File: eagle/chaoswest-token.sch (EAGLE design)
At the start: 40 parts, among them J2 CON_HEADER_PRG_AVR_ICSP-SMD, Q1 Si1967DH, SW1 SSAJ120100, U1 MCP73832T-2ACI/OT, U2 ATTINY85V-10SU, U3 MCP9700AT-E/LT

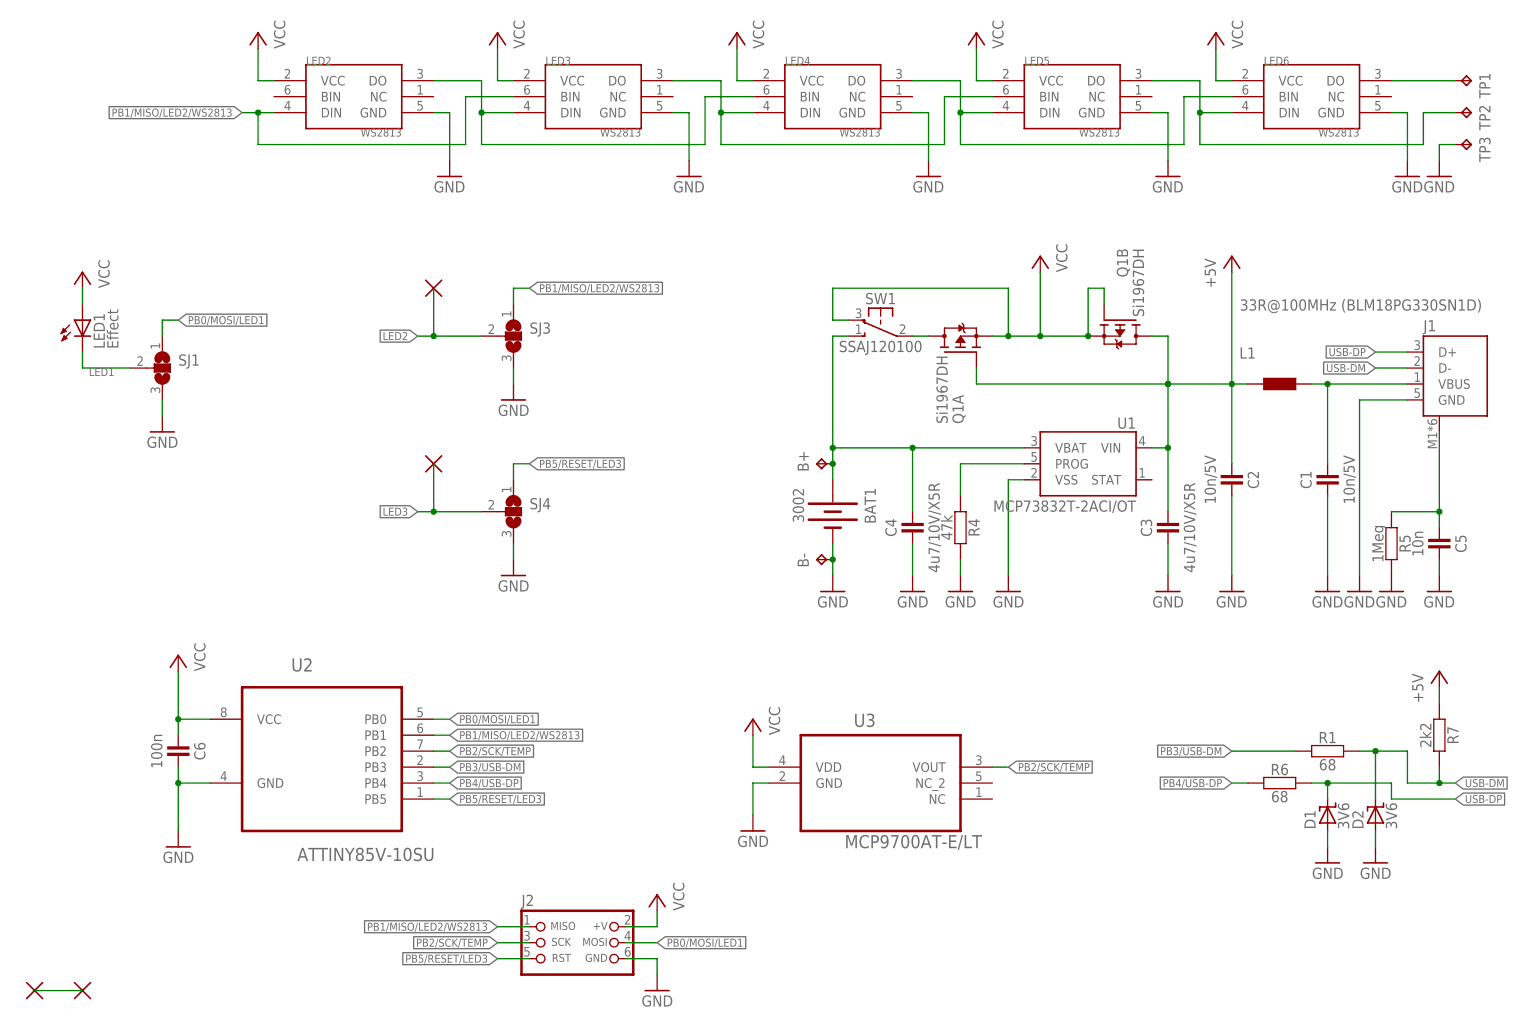
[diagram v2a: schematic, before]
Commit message: routing finished, single layer layout
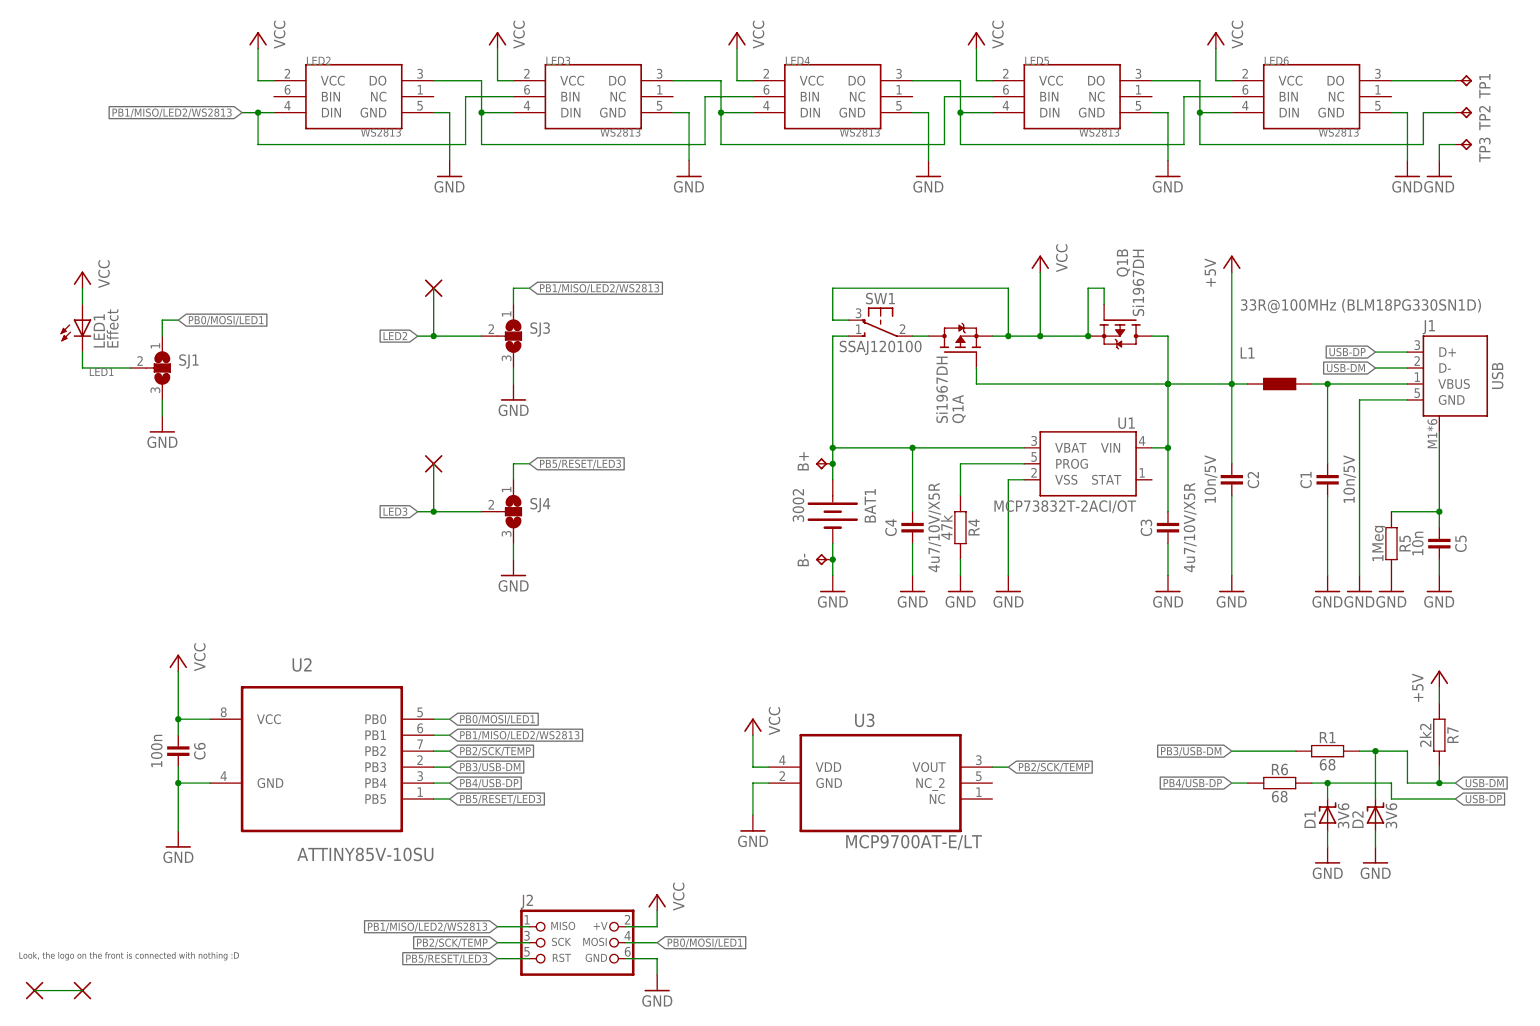
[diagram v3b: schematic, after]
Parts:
- J1: value (none) -> USB
- J2: value CON_HEADER_PRG_AVR_ICSP-SMD -> ISP
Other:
- note added: "Look, the logo on the front is connected with nothing :D"
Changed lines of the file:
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@@
 <layer number="97" name="Info" color="7" fill="1" visible="yes" active="yes"/>
 <layer number="98" name="Guide" color="6" fill="1" visible="yes" active="yes"/>
-<layer number="99" name="SpiceOrder" color="5" fill="1" visible="yes" active="yes"/>
 <layer number="100" name="Muster" color="7" fill="1" visible="no" active="no"/>
-<layer number="101" name="Patch_Top" color="12" fill="4" visible="yes" active="yes"/>
-<layer number="102" name="Vscore" color="7" fill="1" visible="yes" active="yes"/>
-<layer number="103" name="fp3" color="7" fill="1" visible="no" active="yes"/>
-<layer number="104" name="Name" color="7" fill="1" visible="yes" active="yes"/>
-<layer number="105" name="Beschreib" color="9" fill="1" visible="yes" active="yes"/>
-<layer number="106" name="BGA-Top" color="4" fill="1" visible="yes" active="yes"/>
-<layer number="107" name="BD-Top" color="5" fill="1" visible="yes" active="yes"/>
-<layer number="108" name="fp8" color="7" fill="1" visible="no" active="yes"/>
-<layer number="109" name="fp9" color="7" fill="1" visible="no" active="yes"/>
-<layer number="110" name="fp0" color="7" fill="1" visible="no" active="yes"/>
-<layer number="111" name="LPC17xx" color="7" fill="1" visible="yes" active="yes"/>
-<layer number="112" name="tSilk" color="7" fill="1" visible="yes" active="yes"/>
-<layer number="113" name="FRNTTEKEN" color="7" fill="1" visible="yes" active="yes"/>
-<layer number="114" name="FRNTMAAT1" color="7" fill="1" visible="yes" active="yes"/>
-<layer number="115" name="FRNTMAAT2" color="7" fill="1" visible="yes" active="yes"/>
-<layer number="116" name="Patch_BOT" color="9" fill="4" visible="yes" active="yes"/>
-<layer number="117" name="BACKMAAT1" color="7" fill="1" visible="yes" active="yes"/>
-<layer number="118" name="BACKMAAT2" color="7" fill="1" visible="yes" active="yes"/>
-<layer number="119" name="KAP_TEKEN" color="7" fill="1" visible="yes" active="yes"/>
-<layer number="120" name="KAP_MAAT1" color="7" fill="1" visible="yes" active="yes"/>
-<layer number="121" name="_tsilk" color="7" fill="1" visible="yes" active="yes"/>
-<layer number="122" name="_bsilk" color="7" fill="1" visible="yes" active="yes"/>
-<layer number="123" name="tTestmark" color="7" fill="1" visible="no" active="yes"/>
-<layer number="124" name="bTestmark" color="7" fill="1" visible="no" active="yes"/>
-<layer number="125" name="_tNames" color="7" fill="1" visible="yes" active="yes"/>
-<layer number="126" name="_bNames" color="7" fill="1" visible="yes" active="yes"/>
-<layer number="127" name="_tValues" color="7" fill="1" visible="yes" active="yes"/>
-<layer number="128" name="_bValues" color="7" fill="1" visible="yes" active="yes"/>
-<layer number="129" name="Mask" color="7" fill="1" visible="yes" active="yes"/>
-<layer number="130" name="SMDSTROOK" color="7" fill="1" visible="yes" active="yes"/>
-<layer number="131" name="tAdjust" color="7" fill="1" visible="no" active="yes"/>
-<layer number="132" name="bAdjust" color="7" fill="1" visible="no" active="yes"/>
-<layer number="144" name="Drill_legend" color="7" fill="1" visible="yes" active="yes"/>
-<layer number="150" name="Notes" color="7" fill="1" visible="no" active="yes"/>
-<layer number="151" name="HeatSink" color="7" fill="1" visible="yes" active="yes"/>
-<layer number="152" name="_bDocu" color="7" fill="1" visible="yes" active="yes"/>
 <layer number="153" name="FabDoc1" color="6" fill="1" visible="no" active="no"/>
 <layer number="154" name="FabDoc2" color="2" fill="1" visible="no" active="no"/>
 <layer number="155" name="FabDoc3" color="7" fill="15" visible="no" active="no"/>
-<layer number="199" name="Contour" color="7" fill="1" visible="yes" active="yes"/>
-<layer number="200" name="200bmp" color="1" fill="10" visible="yes" active="yes"/>
 <layer number="201" name="201bmp" color="2" fill="1" visible="no" active="no"/>
 <layer number="202" name="202bmp" color="3" fill="1" visible="no" active="no"/>
-<layer number="203" name="203bmp" color="4" fill="10" visible="yes" active="yes"/>
-<layer number="204" name="204bmp" color="5" fill="10" visible="yes" active="yes"/>
-<layer number="205" name="205bmp" color="6" fill="10" visible="yes" active="yes"/>
-<layer number="206" name="206bmp" color="7" fill="10" visible="yes" active="yes"/>
-<layer number="207" name="207bmp" color="8" fill="10" visible="yes" active="yes"/>
-<layer number="208" name="208bmp" color="9" fill="10" visible="yes" active="yes"/>
-<layer number="209" name="209bmp" color="7" fill="1" visible="no" active="yes"/>
-<layer number="210" name="210bmp" color="7" fill="1" visible="no" active="yes"/>
-<layer number="211" name="211bmp" color="7" fill="1" visible="yes" active="yes"/>
-<layer number="212" name="212bmp" color="7" fill="1" visible="yes" active="yes"/>
-<layer number="213" name="213bmp" color="7" fill="1" visible="yes" active="yes"/>
-<layer number="214" name="214bmp" color="7" fill="1" visible="yes" active="yes"/>
-<layer number="215" name="215bmp" color="7" fill="1" visible="yes" active="yes"/>
-<layer number="216" name="216bmp" color="7" fill="1" visible="yes" active="yes"/>
 <layer number="217" name="217bmp" color="18" fill="1" visible="no" active="no"/>
 <layer number="218" name="218bmp" color="19" fill="1" visible="no" active="no"/>
@@
 <layer number="223" name="223bmp" color="24" fill="1" visible="no" active="no"/>
 <layer number="224" name="224bmp" color="25" fill="1" visible="no" active="no"/>
-<layer number="225" name="225bmp" color="7" fill="1" visible="yes" active="yes"/>
-<layer number="226" name="226bmp" color="7" fill="1" visible="yes" active="yes"/>
-<layer number="227" name="227bmp" color="7" fill="1" visible="yes" active="yes"/>
-<layer number="228" name="228bmp" color="7" fill="1" visible="yes" active="yes"/>
-<layer number="229" name="229bmp" color="7" fill="1" visible="yes" active="yes"/>
-<layer number="230" name="230bmp" color="7" fill="1" visible="yes" active="yes"/>
-<layer number="231" name="231bmp" color="7" fill="1" visible="yes" active="yes"/>
-<layer number="248" name="Housing" color="7" fill="1" visible="yes" active="yes"/>
-<layer number="249" name="Edge" color="7" fill="1" visible="yes" active="yes"/>
 <layer number="250" name="Descript" color="7" fill="1" visible="no" active="no"/>
 <layer number="251" name="SMDround" color="7" fill="1" visible="no" active="no"/>
-<layer number="254" name="cooling" color="7" fill="1" visible="yes" active="yes"/>
-<layer number="255" name="Accent" color="7" fill="1" visible="yes" active="yes"/>
 </layers>
 <schematic xreflabel="%F%N/%S.%C%R" xrefpart="/%S.%C%R">
@@
 <part name="U$1" library="extra" deviceset="EMPTY_SIGNAL" device=""/>
 <part name="U$2" library="extra" deviceset="EMPTY_SIGNAL" device=""/>
-<part name="J1" library="Molex-47346-0001" deviceset="47346-0001" device=""/>
+<part name="J1" library="Molex-47346-0001" deviceset="47346-0001" device="" value="USB"/>
 <part name="GND1" library="supply1" deviceset="GND" device=""/>
 <part name="SJ1" library="jumper" deviceset="SJ2W" device=""/>
@@
 <part name="P+5" library="supply1" deviceset="+5V" device=""/>
 <part name="P+6" library="supply1" deviceset="+5V" device=""/>
-<part name="J2" library="dp_devices" deviceset="CON_HEADER_PRG_AVR_ICSP" device="-SMD"/>
+<part name="J2" library="dp_devices" deviceset="CON_HEADER_PRG_AVR_ICSP" device="-SMD" value="ISP"/>
 <part name="P+4" library="supply1" deviceset="VCC" device=""/>
 <part name="GND9" library="supply1" deviceset="GND" device=""/>
@@
 <sheet>
 <plain>
+<text x="7.62" y="15.24" size="1.016" layer="97">Look, the logo on the front is connected with nothing :D</text>
 </plain>
 <instances>

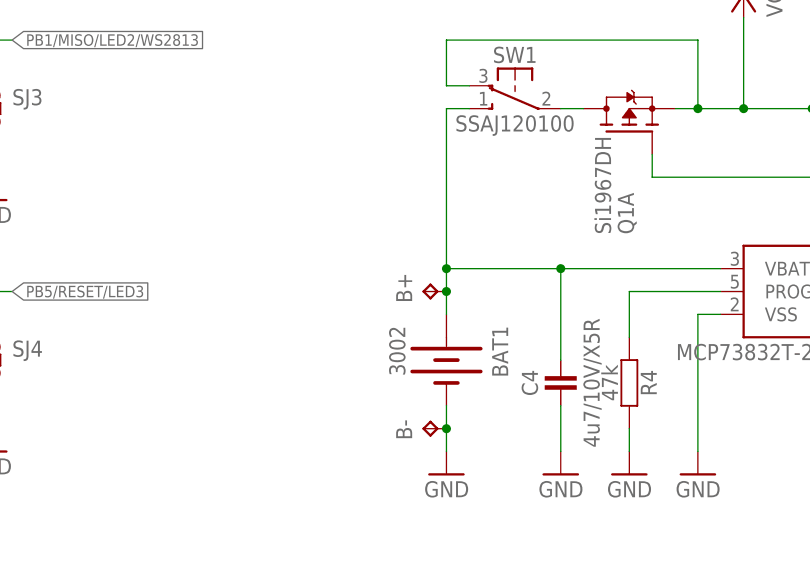
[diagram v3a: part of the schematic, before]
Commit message: put the bottom silk screen (component names) into place
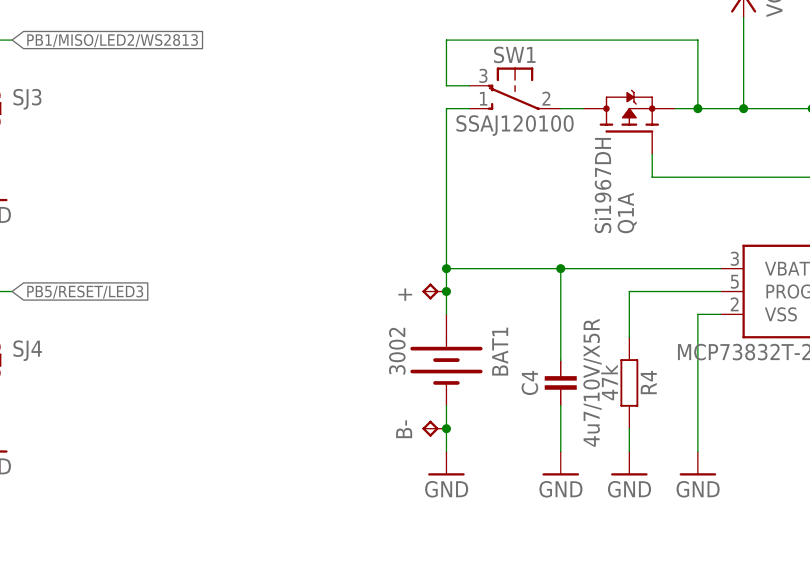
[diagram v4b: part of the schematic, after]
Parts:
- renumbered B+ to +
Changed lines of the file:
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@@
 <part name="GND47" library="supply1" deviceset="GND" device=""/>
 <part name="BAT1" library="extra" deviceset="3002" device=""/>
-<part name="B+" library="testpad" deviceset="TP" device="TP18SQ"/>
+<part name="+" library="testpad" deviceset="TP" device="TP18SQ"/>
 <part name="B-" library="testpad" deviceset="TP" device="TP18SQ"/>
 <part name="U$1" library="extra" deviceset="EMPTY_SIGNAL" device=""/>
@@
 <instance part="GND47" gate="1" x="149.86" y="73.66" rot="MR0"/>
 <instance part="BAT1" gate="G$1" x="137.16" y="86.36" rot="R270"/>
-<instance part="B+" gate="G$1" x="134.62" y="93.98" rot="R90"/>
+<instance part="+" gate="G$1" x="134.62" y="93.98" rot="R90"/>
 <instance part="B-" gate="G$1" x="134.62" y="78.74" rot="R90"/>
 <instance part="U$1" gate="G$1" x="10.16" y="10.16"/>
@@
 <pinref part="BAT1" gate="G$1" pin="+"/>
 <wire x1="137.16" y1="91.44" x2="137.16" y2="93.98" width="0.1524" layer="91"/>
-<pinref part="B+" gate="G$1" pin="TP"/>
+<pinref part="+" gate="G$1" pin="TP"/>
 <wire x1="137.16" y1="93.98" x2="137.16" y2="96.52" width="0.1524" layer="91"/>
 <junction x="137.16" y="93.98"/>
